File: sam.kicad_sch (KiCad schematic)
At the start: 57 parts, among them IC1 HYB4116, IC15 MC6883, IC16 74LS244N, IC2 HYB4116, IC3 HYB4116, IC31 74LS02N, IC33 74LS138N, IC4 HYB4116, IC5 HYB4116, IC6 HYB4116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

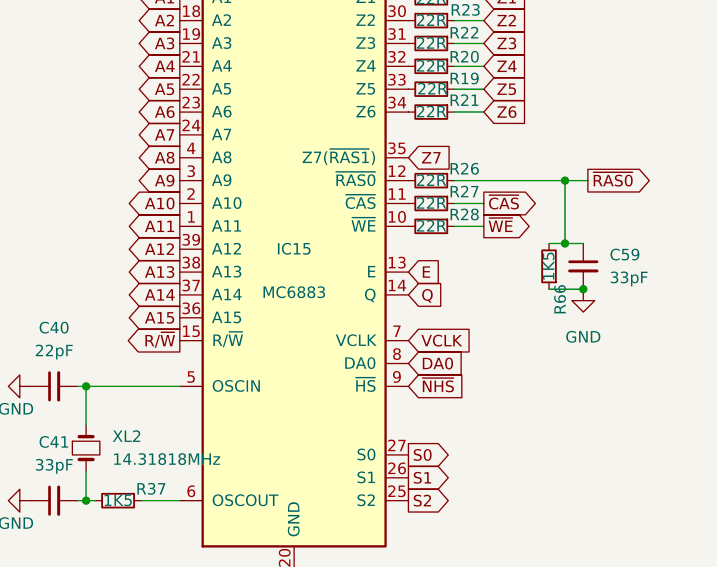
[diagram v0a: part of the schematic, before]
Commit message: label pins
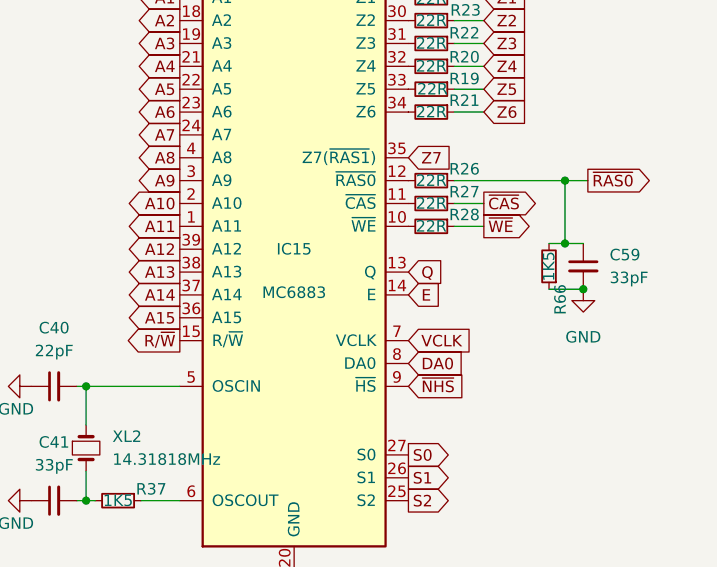
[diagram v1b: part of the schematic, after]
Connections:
- net E: now also IC15.14 (E); no longer IC15.13 (E)
- net Q: now also IC15.13 (Q); no longer IC15.14 (Q)
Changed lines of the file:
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@@
-    )
-  )
-  (global_label "E" (shape input) (at 257.556 62.611 0) (fields_autoplaced)
-    (effects (font (size 1.27 1.27)) (justify left))
-    (property "Intersheet References" "${INTERSHEET_REFS}" (id 0) (at 261.0292 62.5316 0)
-      (effects (font (size 1.27 1.27)) (justify left) hide)
     )
   )
@@
     )
   )
-  (global_label "Q" (shape input) (at 257.556 65.151 0) (fields_autoplaced)
-    (effects (font (size 1.27 1.27)) (justify left))
-    (property "Intersheet References" "${INTERSHEET_REFS}" (id 0) (at 261.2107 65.0716 0)
-      (effects (font (size 1.27 1.27)) (justify left) hide)
-    )
-  )
   (global_label "A4" (shape output) (at 232.156 39.751 180) (fields_autoplaced)
     (effects (font (size 1.27 1.27)) (justify right))
@@
     )
   )
+  (global_label "E" (shape input) (at 257.556 65.151 0) (fields_autoplaced)
+    (effects (font (size 1.27 1.27)) (justify left))
+    (property "Intersheet References" "${INTERSHEET_REFS}" (id 0) (at 261.0292 65.0716 0)
+      (effects (font (size 1.27 1.27)) (justify left) hide)
+    )
+  )
   (global_label "RAM VDD" (shape passive) (at 151.257 24.765 180) (fields_autoplaced)
     (effects (font (size 1.27 1.27)) (justify right))
@@
     )
   )
+  (global_label "Q" (shape input) (at 257.556 62.611 0) (fields_autoplaced)
+    (effects (font (size 1.27 1.27)) (justify left))
+    (property "Intersheet References" "${INTERSHEET_REFS}" (id 0) (at 261.2107 62.5316 0)
+      (effects (font (size 1.27 1.27)) (justify left) hide)
+    )
+  )

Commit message: fix edge connector and op-amp
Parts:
- IC15: Alt Value (none) -> SN74LS783N
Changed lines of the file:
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@@
       (effects (font (size 1.27 1.27)) hide)
     )
-    (pin "1")
-    (pin "2")
-    (pin "3")
-    (pin "4")
-    (pin "5")
-    (pin "6")
-    (pin "10")
-    (pin "8")
-    (pin "9")
     (pin "11")
     (pin "12")
     (pin "13")
-    (pin "14")
-    (pin "7")
   )
   (symbol (lib_id "power:GND") (at 88.392 127.508 0) (unit 1)
@@
       (effects (font (size 1.27 1.27)) hide)
     )
-    (pin "1")
-    (pin "2")
-    (pin "3")
     (pin "4")
     (pin "5")
     (pin "6")
-    (pin "10")
-    (pin "8")
-    (pin "9")
-    (pin "11")
-    (pin "12")
-    (pin "13")
-    (pin "14")
-    (pin "7")
   )
   (symbol (lib_id "power:GND") (at 216.027 138.43 270) (mirror x) (unit 1)
@@
     (pin "2")
     (pin "3")
-    (pin "4")
-    (pin "5")
-    (pin "6")
-    (pin "10")
-    (pin "8")
-    (pin "9")
-    (pin "11")
-    (pin "12")
-    (pin "13")
-    (pin "14")
-    (pin "7")
   )
   (symbol (lib_id "Memory_RAM_Siemens:HYB4116") (at 120.777 103.251 0) (unit 1)
@@
       (effects (font (size 1.27 1.27)) hide)
     )
+    (property "Alt Value" "SN74LS783N" (id 5) (at 244.856 60.071 0)
+      (effects (font (size 1.27 1.27)) hide)
+    )

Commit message: refresh pcb
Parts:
- IC1, IC15, IC16, IC2, IC3, IC31, IC33, IC4, IC5, IC6, IC7, IC8: SA2120 (none) -> Sheet 1
- IC31: SA2120 (none) -> Sheet 1 (spare)
- JP13-14: value 16k/32k -> 32k/64k
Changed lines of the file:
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@@
+      (effects (font (size 1.27 1.27)) hide)
+    )
+    (property "SA2120" "Sheet 1" (id 5) (at 35.433 42.418 0)
       (effects (font (size 1.27 1.27)) hide)
     )
@@
     (in_bom yes) (on_board yes) (fields_autoplaced)
     (property "Reference" "JP13-14" (id 0) (at 112.903 199.39 0))
-    (property "Value" "16k/32k" (id 1) (at 112.903 201.93 0))
+    (property "Value" "32k/64k" (id 1) (at 112.903 201.93 0))
     (property "Footprint" "Connector_PinHeader_2.54mm:PinHeader_1x03_P2.54mm_Vertical" (id 2) (at 112.903 195.707 0)
       (effects (font (size 1.27 1.27)) hide)
@@
     )
     (property "Note" "use general 4164 with suitable timing" (id 4) (at 120.777 42.545 0)
+      (effects (font (size 1.27 1.27)) hide)
+    )
+    (property "SA2120" "Sheet 1" (id 5) (at 120.777 42.545 0)
       (effects (font (size 1.27 1.27)) hide)
     )
@@
     )
     (property "DigiKey" "296-1653-5-ND" (id 4) (at 35.306 168.91 0)
+      (effects (font (size 1.27 1.27)) hide)
+    )
+    (property "SA2120" "Sheet 1" (id 5) (at 35.306 168.91 0)
       (effects (font (size 1.27 1.27)) hide)
     )
@@
       (effects (font (size 1.27 1.27)) hide)
     )
+    (property "SA2120" "Sheet 1" (id 5) (at 100.838 176.276 0)
+      (effects (font (size 1.27 1.27)) hide)
+    )
     (pin "11")
     (pin "12")
@@
     )
     (property "DigiKey" "296-1639-5-ND" (id 4) (at 122.047 166.116 0)
+      (effects (font (size 1.27 1.27)) hide)
+    )
+    (property "SA2120" "Sheet 1" (id 5) (at 122.047 166.116 0)
       (effects (font (size 1.27 1.27)) hide)
     )
@@
       (effects (font (size 1.27 1.27)) hide)
     )
+    (property "SA2120" "Sheet 1" (id 5) (at 78.105 42.418 0)
+      (effects (font (size 1.27 1.27)) hide)
+    )
     (pin "1")
     (pin "10")
@@
       (effects (font (size 1.27 1.27)) hide)
     )
+    (property "SA2120" "Sheet 1" (id 5) (at 236.22 124.333 0)
+      (effects (font (size 1.27 1.27)) hide)
+    )
     (pin "4")
     (pin "5")
@@
       (effects (font (size 1.27 1.27)) hide)
     )
+    (property "SA2120" "Sheet 1 (spare)" (id 5) (at 98.933 195.707 0)
+      (effects (font (size 1.27 1.27)) hide)
+    )
     (pin "1")
     (pin "2")
@@
     )
     (property "Note" "use general 4164 with suitable timing" (id 4) (at 120.777 103.251 0)
+      (effects (font (size 1.27 1.27)) hide)
+    )
+    (property "SA2120" "Sheet 1" (id 5) (at 120.777 103.251 0)
       (effects (font (size 1.27 1.27)) hide)
     )
@@
       (effects (font (size 1.27 1.27)) hide)
     )
+    (property "SA2120" "Sheet 1" (id 5) (at 35.433 103.124 0)
+      (effects (font (size 1.27 1.27)) hide)
+    )
     (pin "1")
     (pin "10")
@@
       (effects (font (size 1.27 1.27)) hide)
     )
+    (property "SA2120" "Sheet 1" (id 5) (at 163.449 103.251 0)
+      (effects (font (size 1.27 1.27)) hide)
+    )
     (pin "1")
     (pin "10")
@@
       (effects (font (size 1.27 1.27)) hide)
     )
+    (property "SA2120" "Sheet 1" (id 5) (at 163.449 42.545 0)
+      (effects (font (size 1.27 1.27)) hide)
+    )
     (pin "1")
     (pin "10")
@@
       (effects (font (size 1.27 1.27)) hide)
     )
+    (property "SA2120" "Sheet 1" (id 5) (at 78.105 103.124 0)
+      (effects (font (size 1.27 1.27)) hide)
+    )
     (pin "1")
     (pin "10")
@@
       (effects (font (size 1.27 1.27)) hide)
     )
+    (property "SA2120" "Sheet 1" (id 6) (at 244.856 60.071 0)
+      (effects (font (size 1.27 1.27)) hide)
+    )
